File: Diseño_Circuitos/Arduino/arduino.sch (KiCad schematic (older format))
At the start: 22 parts

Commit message: schematic completed
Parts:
- added C6, C7, C8, C9: 100nF, symbol C_Small
- added D1, D2, D3, D4: LED_ALT, symbol LED_ALT
- added D5: LED_RCGB, symbol LED_RCGB
- added J5, J6: Conn_02x03_Counter_Clockwise, symbol Conn_02x03_Counter_Clockwise
- added R1, R2, R3, R4, R5, R6, R7: 330, symbol R_Small
- added R10, R13, R14, R9: 10K, symbol R_Small
- added SW2, SW3, SW4, SW5: SW_Push, symbol SW_Push
- gave numbers to parts that had none: 22
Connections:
- net +3V3: now also C6.1, C7.1, C8.1, C9.1, J5.6 (Pin_6), J6.6 (Pin_6), SW2.2, SW3.2, SW4.2, SW5.2
- net BTN1: now also C6.2, R9.2, SW2.1
- net BTN2: now also C7.2, R10.2, SW3.1
- net BTN3: now also C8.2, R13.2, SW4.1
- net BTN4: now also C9.2, R14.2, SW5.1
- net BT_RX: now also R4.2
- net BT_TX: now also R5.2
- net GND: now also D1.1 (K), D2.1 (K), D3.1 (K), D4.1 (K), D5.2 (K), J5.4 (Pin_4), J6.4 (Pin_4), R10.1, R13.1, R14.1, R9.1
- net LED1: now also R7.2
- net LED2: now also R6.2
- net LED_B: now also R3.2
- net LED_G: now also R2.2
- net LED_R: now also R1.2
- net MISO: now also J5.1 (Pin_1)
- net MOSI: now also J5.5 (Pin_5)
- net PDI_DATA: now also J6.1 (Pin_1)
- net RESET: now also J5.3 (Pin_3), J6.3 (Pin_3)
- net SCK: now also J5.2 (Pin_2)
- new net: D1.2 (A), R4.1
- new net: D2.2 (A), R5.1
- new net: D3.2 (A), R6.1
- new net: D4.2 (A), R7.1
- new net: D5.1 (RA), R1.1
- new net: D5.3 (GA), R2.1
- new net: D5.4 (BA), R3.1
- no-connect marks 12 -> 14
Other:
- note added: "BUTTONS"
- note added: "LEDS"
- note added: "PDI TARGET\n"
- note added: "SPI TARGET\n"

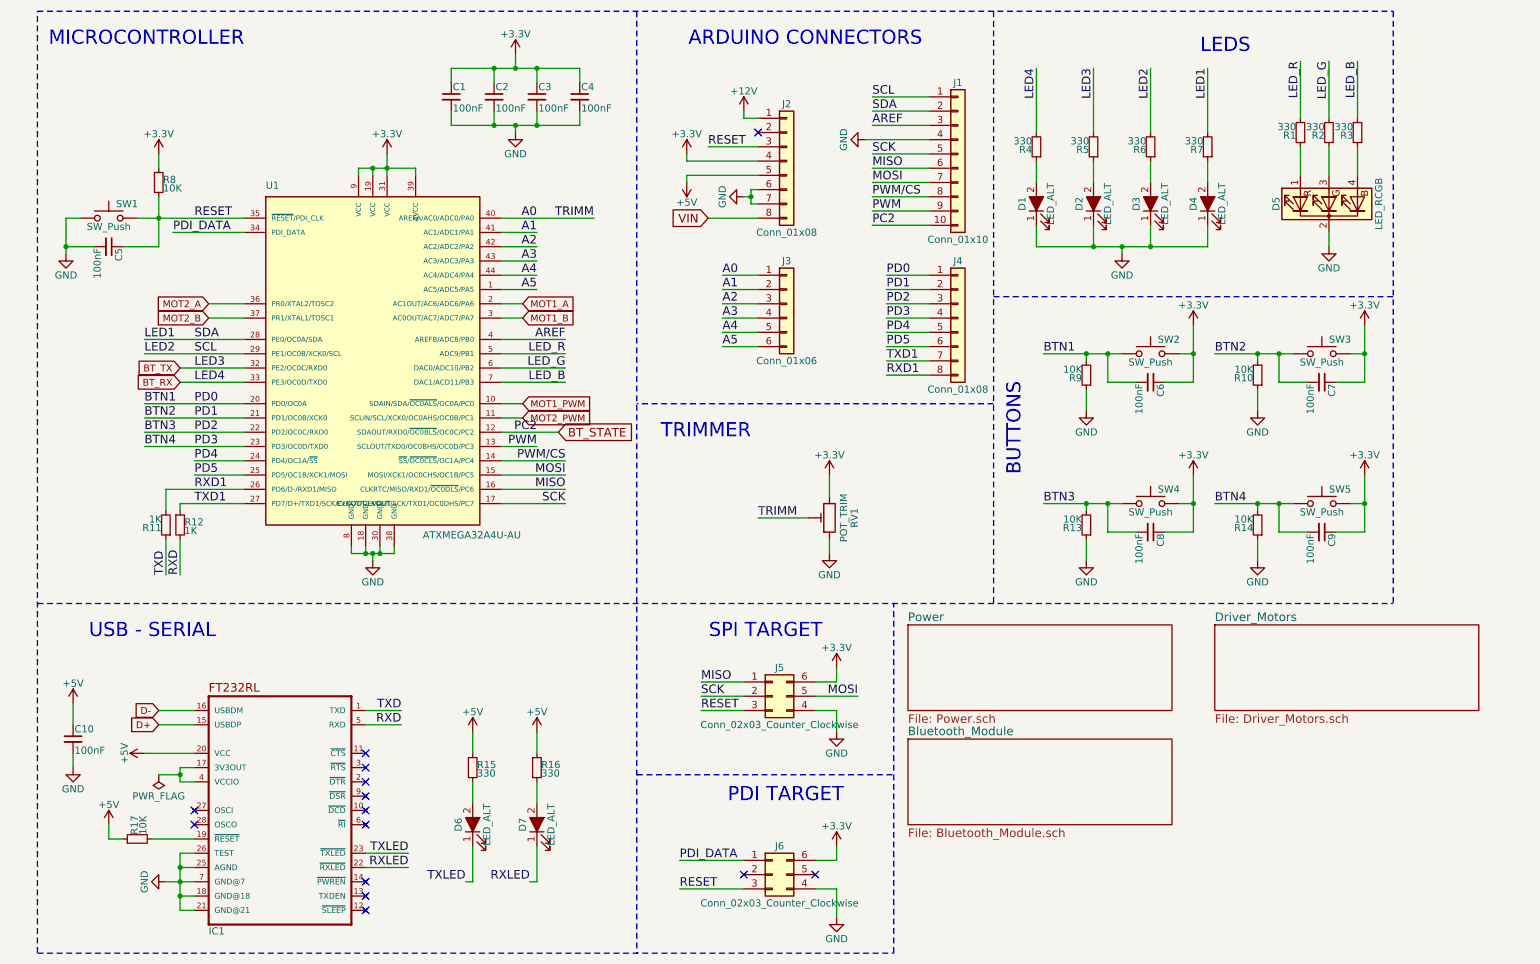
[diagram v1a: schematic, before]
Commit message: pcb components placed
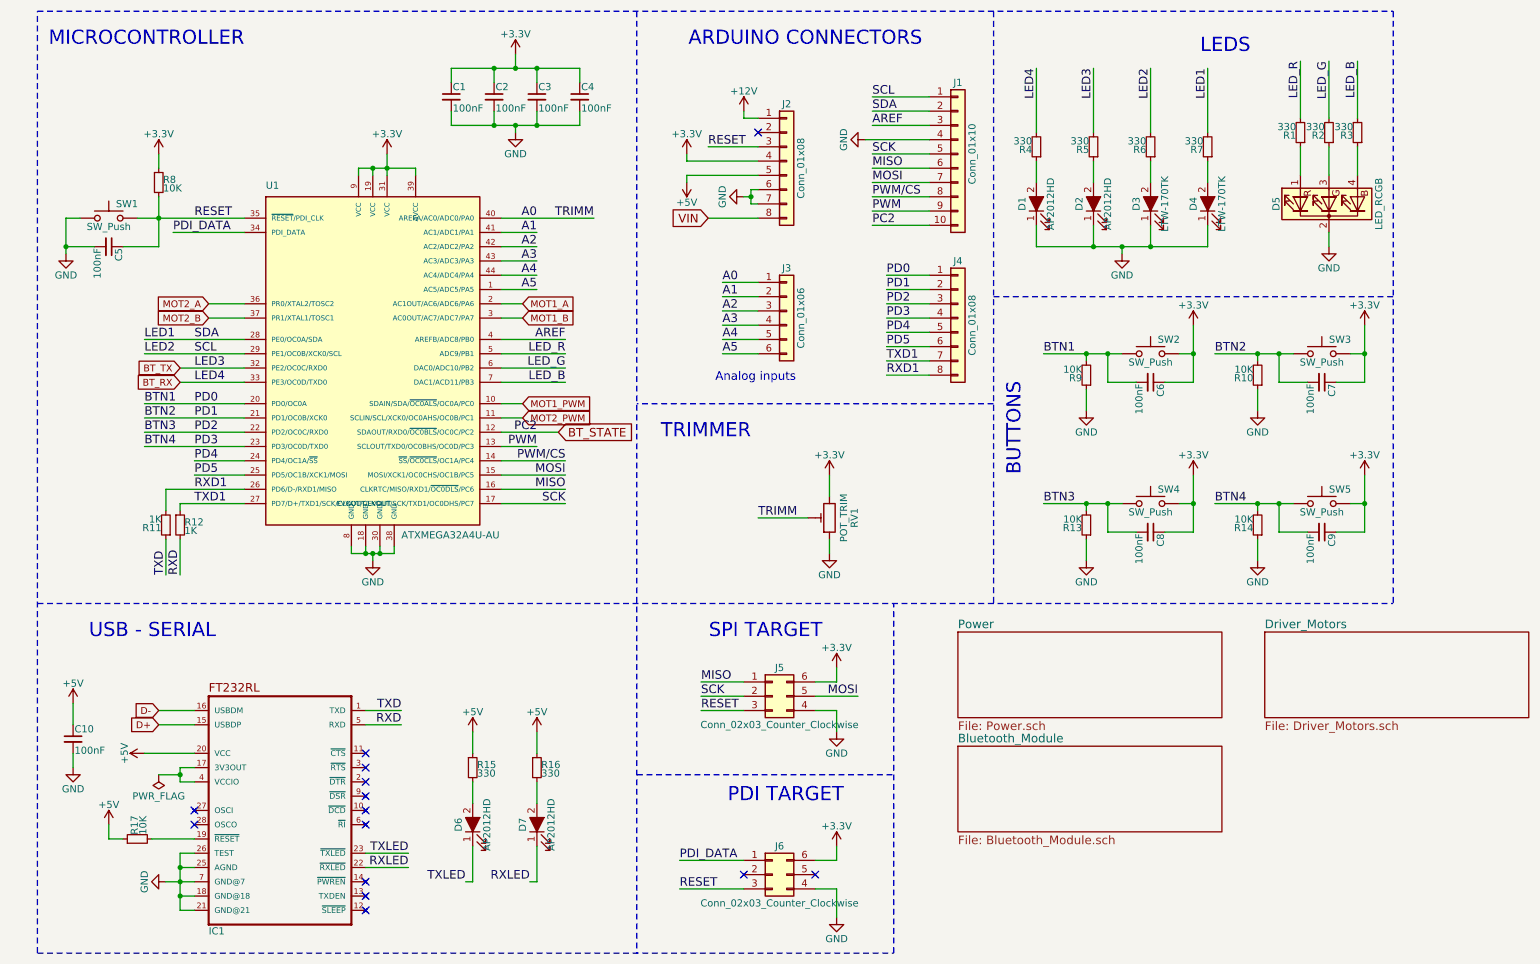
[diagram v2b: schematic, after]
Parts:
- C1, C10, C2, C3, C4, C5, C6, C7, C8, C9: footprint (none) -> custom footprints:C_0805_HandSoldering
- D1, D2, D6, D7: value LED_ALT -> AP2012HD; footprint (none) -> custom footprints:LED_0805
- D3, D4: value LED_ALT -> LTW-170TK; footprint (none) -> custom footprints:LED_0805
- D5: footprint (none) -> custom footprints:LED_150080M153000
- IC1: footprint SSOP28-LD -> custom footprints:SSOP28-LD
- J1: footprint (none) -> custom footprints:Pin_Header_Straight_1x10_Pitch2.54mm
- J2, J4: footprint (none) -> custom footprints:Pin_Header_Straight_1x08_Pitch2.54mm
- J3: footprint (none) -> custom footprints:Pin_Header_Straight_1x06_Pitch2.54mm
- J5, J6: footprint (none) -> custom footprints:Pin_Header_Straight_2x03_Pitch2.54mm
- R1, R10, R11, R12, R13, R14, R15, R16, R17, R2, R3, R4, R5, R6, R7, R8, R9: footprint (none) -> custom footprints:R_0805_HandSoldering
- RV1: footprint (none) -> custom footprints:Potentiometer_Trimmer_Bourns_PV36W
- SW1, SW2, SW3, SW4, SW5: footprint (none) -> custom footprints:SW_SPST_FSMSM
- U1: footprint TQFP44 -> custom footprints:ATXMEGA32A4U-AU
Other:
- note added: "Analog inputs"
- moved on the sheet: J3

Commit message: pcb buttons and outputs traced
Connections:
- net +3V3: now also J5.2 (Pin_2), J6.2 (Pin_2); no longer J5.6 (Pin_6), J6.6 (Pin_6)
- net GND: now also J5.6 (Pin_6), J6.6 (Pin_6); no longer J5.4 (Pin_4), J6.4 (Pin_4)
- net MOSI: now also J5.4 (Pin_4); no longer J5.5 (Pin_5)
- net RESET: now also J5.5 (Pin_5), J6.5 (Pin_5); no longer J5.3 (Pin_3), J6.3 (Pin_3)
- net SCK: now also J5.3 (Pin_3); no longer J5.2 (Pin_2)
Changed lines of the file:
@@
 	1    0    0    -1
 $EndComp
-NoConn ~ 6050 6650
-NoConn ~ 5550 6650
 Text Label 5250 5300 0    60   ~ 0
 MISO
-Text Label 5250 5400 0    60   ~ 0
+Text Label 5250 5500 0    60   ~ 0
 SCK
+Text Label 6350 5500 2    60   ~ 0
+MOSI
 Text Label 6350 5400 2    60   ~ 0
-MOSI
-Text Label 5250 5500 0    60   ~ 0
 RESET
 $Comp
 L +3.3V #PWR031
 U 1 1 5F7548F7
-P 6200 5200
-F 0 "#PWR031" H 6200 5050 50  0001 C CNN
-F 1 "+3.3V" H 6200 5340 50  0000 C CNN
-F 2 "" H 6200 5200 50  0001 C CNN
-F 3 "" H 6200 5200 50  0001 C CNN
-	1    6200 5200
-	1    0    0    -1
+P 5300 5400
+F 0 "#PWR031" H 5300 5250 50  0001 C CNN
+F 1 "+3.3V" H 5300 5540 50  0000 C CNN
+F 2 "" H 5300 5400 50  0001 C CNN
+F 3 "" H 5300 5400 50  0001 C CNN
+	1    5300 5400
+	0    -1   -1   0
 $EndComp
 $Comp
 L GND #PWR032
 U 1 1 5F754992
-P 6200 5650
-F 0 "#PWR032" H 6200 5400 50  0001 C CNN
-F 1 "GND" H 6200 5500 50  0000 C CNN
-F 2 "" H 6200 5650 50  0001 C CNN
-F 3 "" H 6200 5650 50  0001 C CNN
-	1    6200 5650
-	1    0    0    -1
+P 6350 5300
+F 0 "#PWR032" H 6350 5050 50  0001 C CNN
+F 1 "GND" H 6350 5150 50  0000 C CNN
+F 2 "" H 6350 5300 50  0001 C CNN
+F 3 "" H 6350 5300 50  0001 C CNN
+	1    6350 5300
+	0    -1   -1   0
 $EndComp
 Wire Wire Line
 	5250 5300 5550 5300
 Wire Wire Line
-	5250 5400 5550 5400
-Wire Wire Line
-	5550 5500 5250 5500
-Wire Wire Line
-	6050 5500 6200 5500
-Wire Wire Line
-	6200 5500 6200 5650
-Wire Wire Line
-	6200 5200 6200 5300
-Wire Wire Line
-	6200 5300 6050 5300
+	5250 5500 5550 5500
 Wire Wire Line
 	6050 5400 6350 5400
+Wire Wire Line
+	6050 5300 6350 5300
+Wire Wire Line
+	6050 5500 6350 5500
 Text Notes 6100 5000 2    99   ~ 0
 SPI TARGET\n
@@
 L +3.3V #PWR033
 U 1 1 5F755A5B
-P 6200 6450
-F 0 "#PWR033" H 6200 6300 50  0001 C CNN
-F 1 "+3.3V" H 6200 6590 50  0000 C CNN
-F 2 "" H 6200 6450 50  0001 C CNN
-F 3 "" H 6200 6450 50  0001 C CNN
-	1    6200 6450
-	1    0    0    -1
+P 5100 6650
+F 0 "#PWR033" H 5100 6500 50  0001 C CNN
+F 1 "+3.3V" H 5100 6790 50  0000 C CNN
+F 2 "" H 5100 6650 50  0001 C CNN
+F 3 "" H 5100 6650 50  0001 C CNN
+	1    5100 6650
+	0    -1   -1   0
 $EndComp
 $Comp
 L GND #PWR034
 U 1 1 5F755AF6
-P 6200 6950
-F 0 "#PWR034" H 6200 6700 50  0001 C CNN
-F 1 "GND" H 6200 6800 50  0000 C CNN
-F 2 "" H 6200 6950 50  0001 C CNN
-F 3 "" H 6200 6950 50  0001 C CNN
-	1    6200 6950
-	1    0    0    -1
+P 6100 6500
+F 0 "#PWR034" H 6100 6250 50  0001 C CNN
+F 1 "GND" H 6100 6350 50  0000 C CNN
+F 2 "" H 6100 6500 50  0001 C CNN
+F 3 "" H 6100 6500 50  0001 C CNN
+	1    6100 6500
+	-1   0    0    1
 $EndComp
-Text Label 5100 6750 0    60   ~ 0
+Text Label 6500 6650 2    60   ~ 0
 RESET
 Text Label 5100 6550 0    60   ~ 0
@@
 	5100 6550 5550 6550
 Wire Wire Line
-	5100 6750 5550 6750
-Wire Wire Line
-	6050 6750 6200 6750
-Wire Wire Line
-	6200 6750 6200 6950
-Wire Wire Line
-	6050 6550 6200 6550
-Wire Wire Line
-	6200 6550 6200 6450
+	6500 6650 6050 6650
 Wire Notes Line
 	6600 7200 6600 4750
@@
 Text Notes 5350 3200 0    60   ~ 0
 Analog inputs
+Wire Wire Line
+	5300 5400 5550 5400
+Wire Wire Line
+	5100 6650 5550 6650
+NoConn ~ 5550 6750
+NoConn ~ 6050 6750
+Wire Wire Line
+	6050 6550 6100 6550
+Wire Wire Line
+	6100 6550 6100 6500
 $EndSCHEMATC
